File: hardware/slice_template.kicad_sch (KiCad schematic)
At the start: 24 parts, among them J1 Conn_01x10_Socket, SW1 SW_DIP_x04, U1 AP63205, U2 PCA9306DC1

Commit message: finished layout
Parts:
- removed C7: 100nF, Capacitor_SMD:C_1206_3216Metric, symbol Device:C_Small
- removed R1, R2: 4.7k, Resistor_SMD:R_0603_1608Metric_Pad0.98x0.95mm_HandSolder, symbol Device:R
- removed R3: 200k, Resistor_SMD:R_0603_1608Metric_Pad0.98x0.95mm_HandSolder, symbol Device:R
- removed U2: PCA9306DC1, Package_SO:VSSOP-8_2.3x2mm_P0.5mm, symbol Interface:PCA9306DC1
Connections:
- net GPIO22 is gone; now on net SYNC/CAN_{INT}: A2.29 (GPIO22)
- net GPIO26_ADC0 is gone; now on net INT/CAN_{CS}: A2.31 (GPIO26_ADC0)
- net I2C_CLK: now also SW1.5
- net I2C_DAT: now also SW1.6
- net INT/CAN_{CS}: no longer A2.4 (GPIO2)
- net LED: now also A2.2 (GPIO1); no longer A2.5 (GPIO3)
- net SYNC/CAN_{INT}: no longer A2.2 (GPIO1)
- net SPI0_MISO/GPIO16 renamed GPIO16
- net SPI0_MOSI/GPIO19 renamed GPIO19
- net SPI0_SCK/GPIO18 renamed GPIO18
- net SPI0_~{CS}/GPIO17 renamed GPIO17
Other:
- note removed: "I2C Level Shifter"
- moved on the sheet: A2, C1, C2, C3, C4, C5, C6, D1, D2, H1, H2, H3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

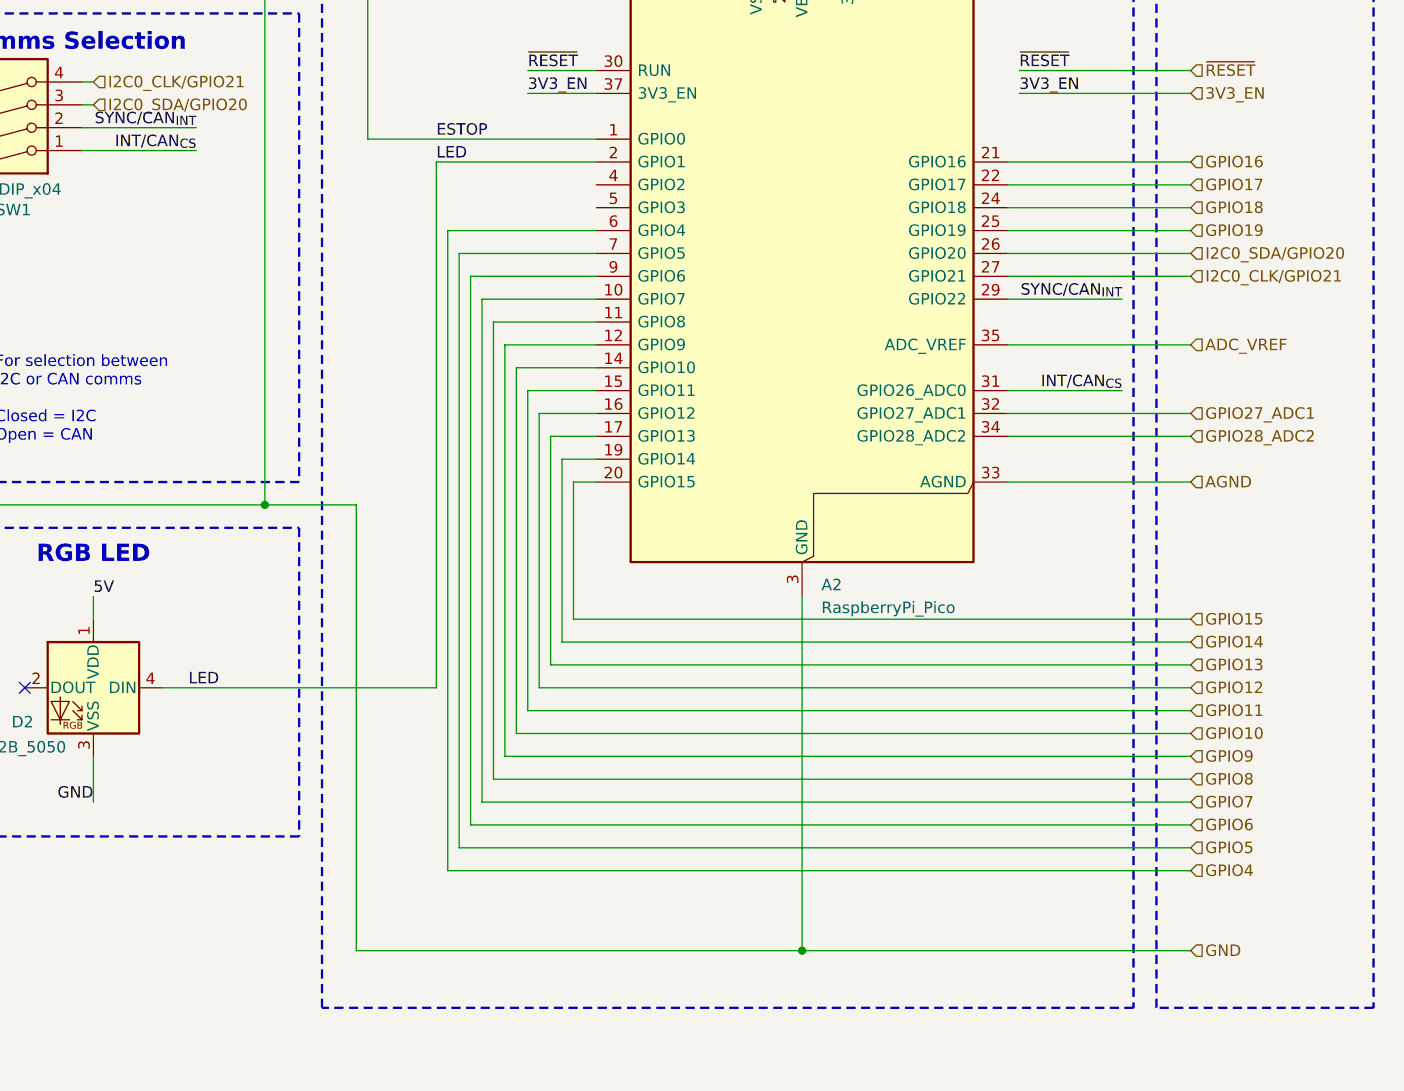
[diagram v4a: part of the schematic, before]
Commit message: added pins 2 and 3 to hierarchical sheet
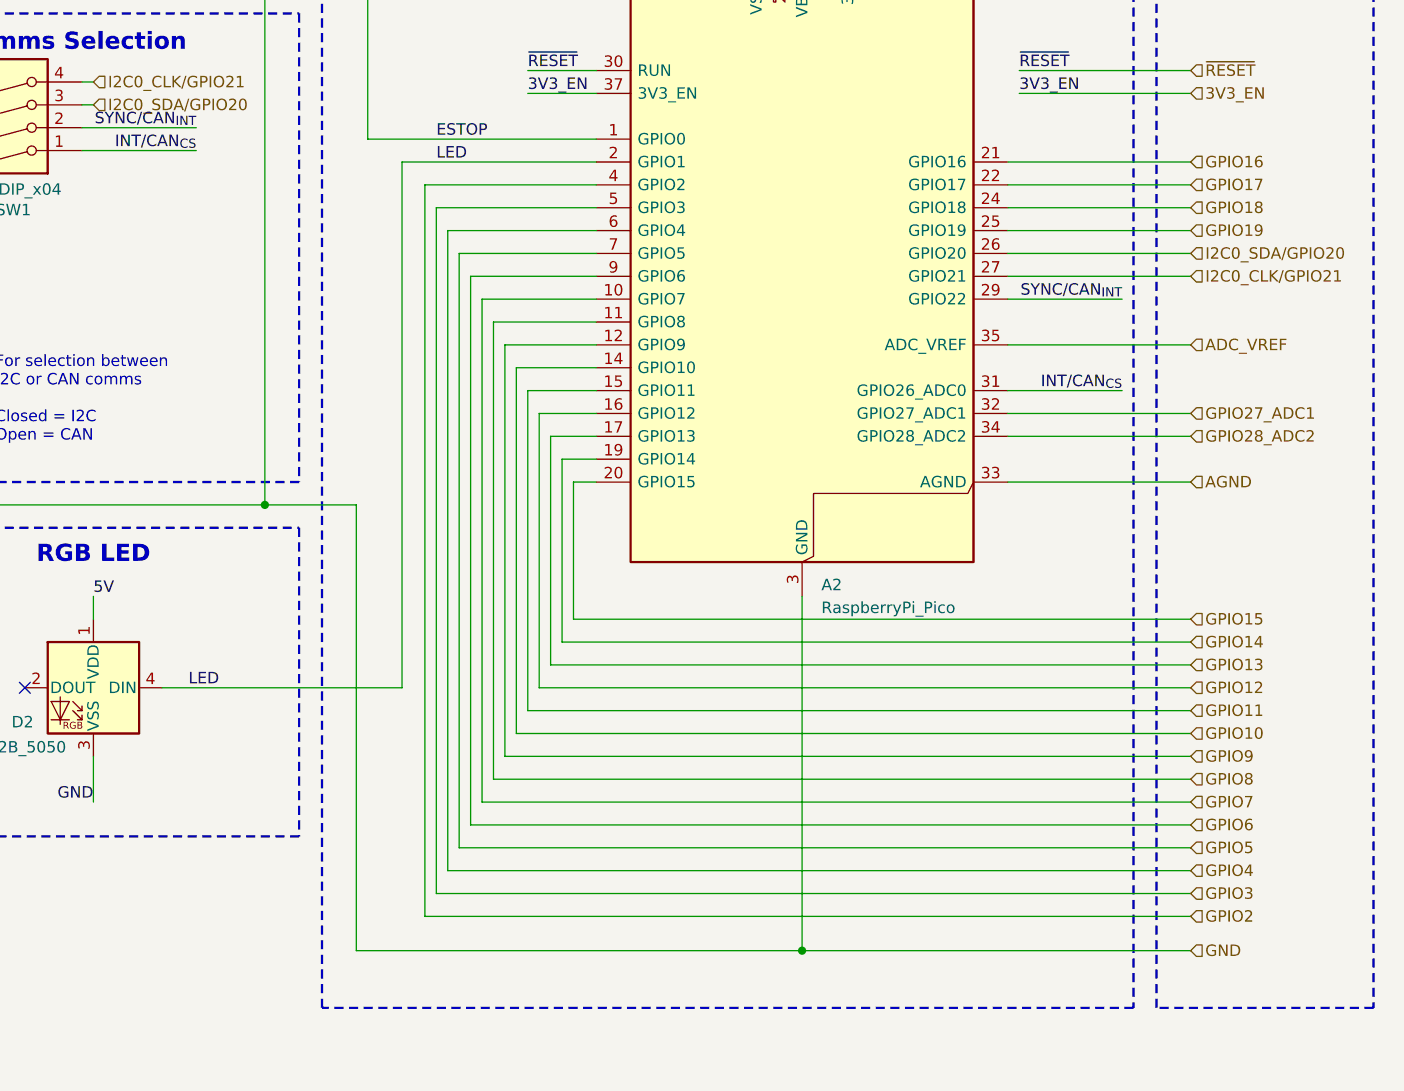
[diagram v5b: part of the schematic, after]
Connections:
- net GPIO2: now reaches A2.4 (GPIO2)
- net GPIO3: now reaches A2.5 (GPIO3)
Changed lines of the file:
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@@
+	(wire
+		(pts
+			(xy 247.65 193.04) (xy 247.65 111.76)
+		)
+		(stroke
+			(width 0)
+			(type default)
+		)
+	)
 	(wire
 		(pts
@@
 	(wire
 		(pts
+			(xy 248.92 190.5) (xy 332.74 190.5)
+		)
+		(stroke
+			(width 0)
+			(type default)
+		)
+	)
+	(wire
+		(pts
 			(xy 257.81 172.72) (xy 332.74 172.72)
 		)
@@
 	(wire
 		(pts
-			(xy 248.92 109.22) (xy 266.7 109.22)
+			(xy 245.11 109.22) (xy 266.7 109.22)
 		)
 		(stroke
@@
 	(wire
 		(pts
+			(xy 248.92 114.3) (xy 248.92 190.5)
+		)
+		(stroke
+			(width 0)
+			(type default)
+		)
+	)
+	(wire
+		(pts
 			(xy 312.42 139.7) (xy 332.74 139.7)
 		)
@@
 	(wire
 		(pts
+			(xy 332.74 193.04) (xy 247.65 193.04)
+		)
+		(stroke
+			(width 0)
+			(type default)
+		)
+	)
+	(wire
+		(pts
 			(xy 209.55 107.95) (xy 222.25 107.95)
 		)
@@
 	(wire
 		(pts
+			(xy 266.7 114.3) (xy 248.92 114.3)
+		)
+		(stroke
+			(width 0)
+			(type default)
+		)
+	)
+	(wire
+		(pts
+			(xy 247.65 111.76) (xy 266.7 111.76)
+		)
+		(stroke
+			(width 0)
+			(type default)
+		)
+	)
+	(wire
+		(pts
 			(xy 289.56 77.47) (xy 289.56 83.82)
 		)
@@
 	(wire
 		(pts
-			(xy 218.44 167.64) (xy 248.92 167.64)
+			(xy 218.44 167.64) (xy 245.11 167.64)
 		)
 		(stroke
@@
 	(wire
 		(pts
-			(xy 248.92 109.22) (xy 248.92 167.64)
+			(xy 245.11 109.22) (xy 245.11 167.64)
 		)
 		(stroke
@@
 		(effects
 			(font
+				(size 1.27 1.27)
+			)
+			(justify left)
+		)
+	)
+	(hierarchical_label "GPIO3"
+		(shape input)
+		(at 332.74 190.5 0)
+		(effects
+			(font
+				(size 1.27 1.27)
+			)
+			(justify left)
+		)
+	)
+	(hierarchical_label "GPIO2"
+		(shape input)
+		(at 332.74 193.04 0)
+		(effects
+			(font
